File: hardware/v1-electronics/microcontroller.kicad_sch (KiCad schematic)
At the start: 8 parts, among them J1 USB_C_Receptacle_USB2.0_14P, U1 MDBT50Q-1MV2

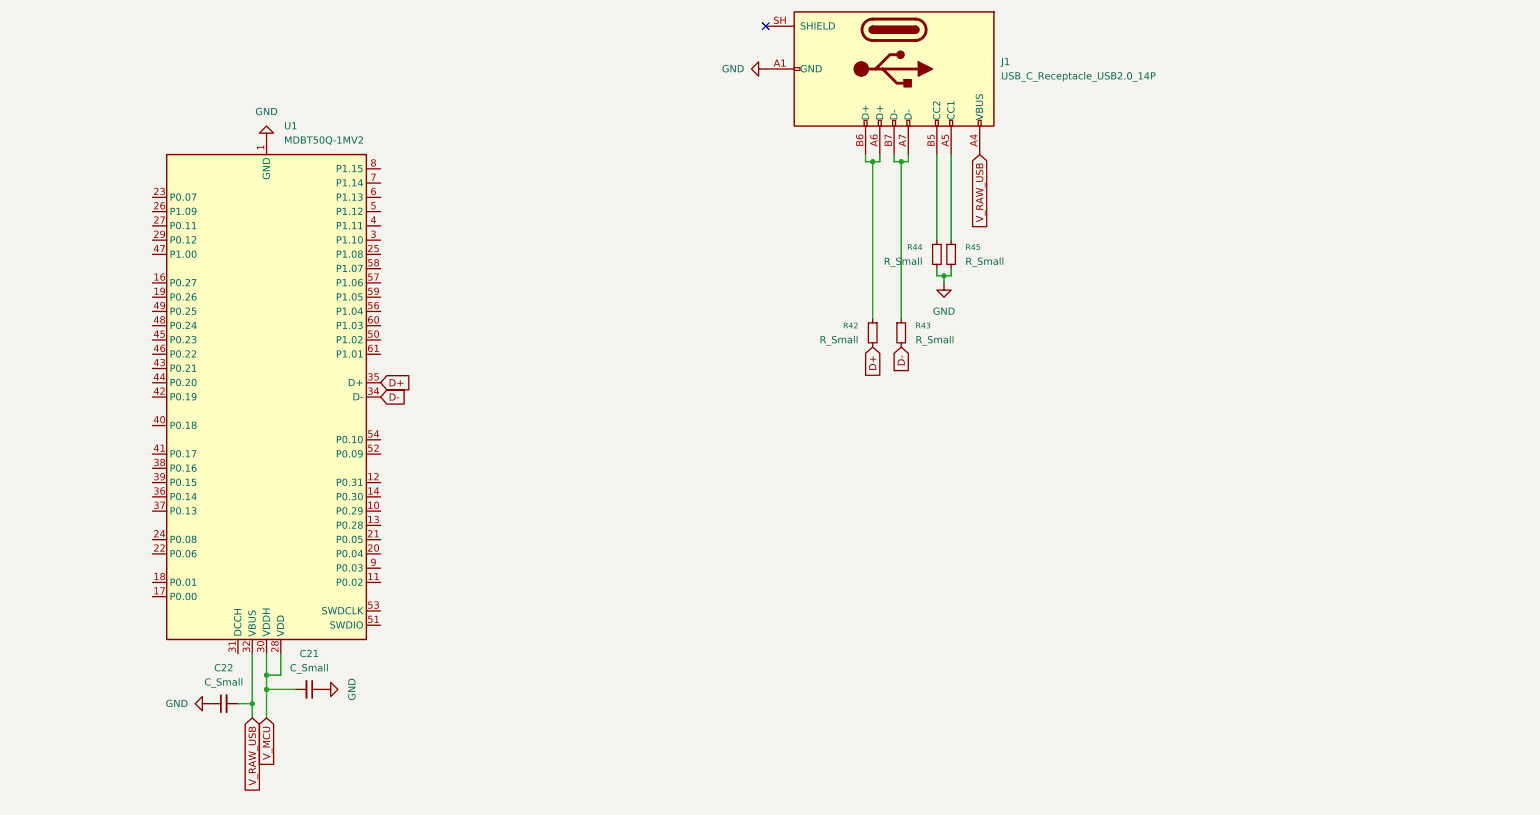
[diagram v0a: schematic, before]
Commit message: feat(v1 hardware): add simple power circuitry
I've added simple power circuitry. It does not do everything I want but
it's a start.
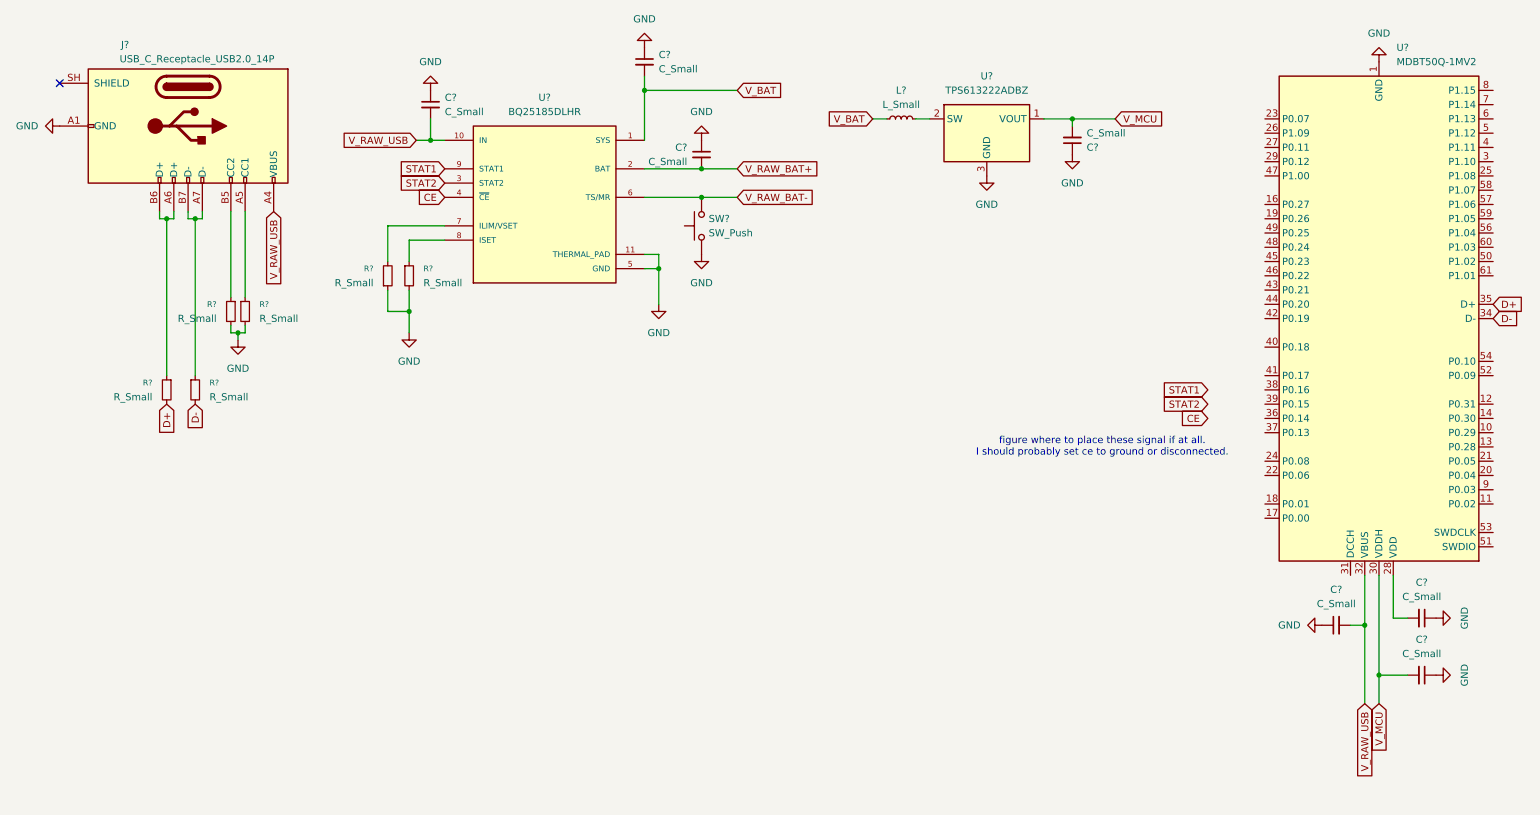
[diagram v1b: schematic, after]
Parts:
- added C? (x5): C_Small, symbol Device:C_Small
- added L?: L_Small, symbol Device:L_Small
- added R? (x2): R_Small, symbol Device:R_Small
- added SW?: SW_Push, symbol Switch:SW_Push
- added U?: TPS613222ADBZ, Package_TO_SOT_SMD:SOT-23, symbol Regulator_Switching:TPS613222ADBZ
- added U?: BQ25185DLHR, BQ25185DLHR:IC_BQ25185DLHR, symbol TI BQ25185DLHR:BQ25185DLHR
- renumbered C22 to C?, C21 to C?, J1 to J?, R42 to R?, R43 to R?, R44 to R?, R45 to R?, U1 to U?
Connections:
- net GND: now also C?.1, C?.1, C?.1, C?.1, C?.1, R?.1, R?.2, SW?.1, U?.11 (THERMAL_PAD), U?.3 (GND), U?.5 (GND)
- net V_MCU: now also C?.2, U?.1 (VOUT); no longer U?.28 (VDD)
- net V_RAW_USB: now also C?.2, U?.10 (IN)
- new net: R?.1, U?.8 (ISET)
- new net: R?.2, U?.7 (ILIM/VSET)
- new net: L?.2, U?.2 (SW)
- new net: C?.2, U?.28 (VDD)
- new net CE: U?.4 (~{CE})
- new net STAT1: U?.9 (STAT1)
- new net STAT2: U?.3 (STAT2)
- new net V_BAT: C?.2, L?.1, U?.1 (SYS)
- new net V_RAW_BAT+: C?.2, U?.2 (BAT)
- new net V_RAW_BAT-: SW?.2, U?.6 (TS/MR)
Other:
- note added: "figure where to place these signal if at all. I should probably set ce to ground or disconnected."
- moved on the sheet: C?, J?, R?, U?

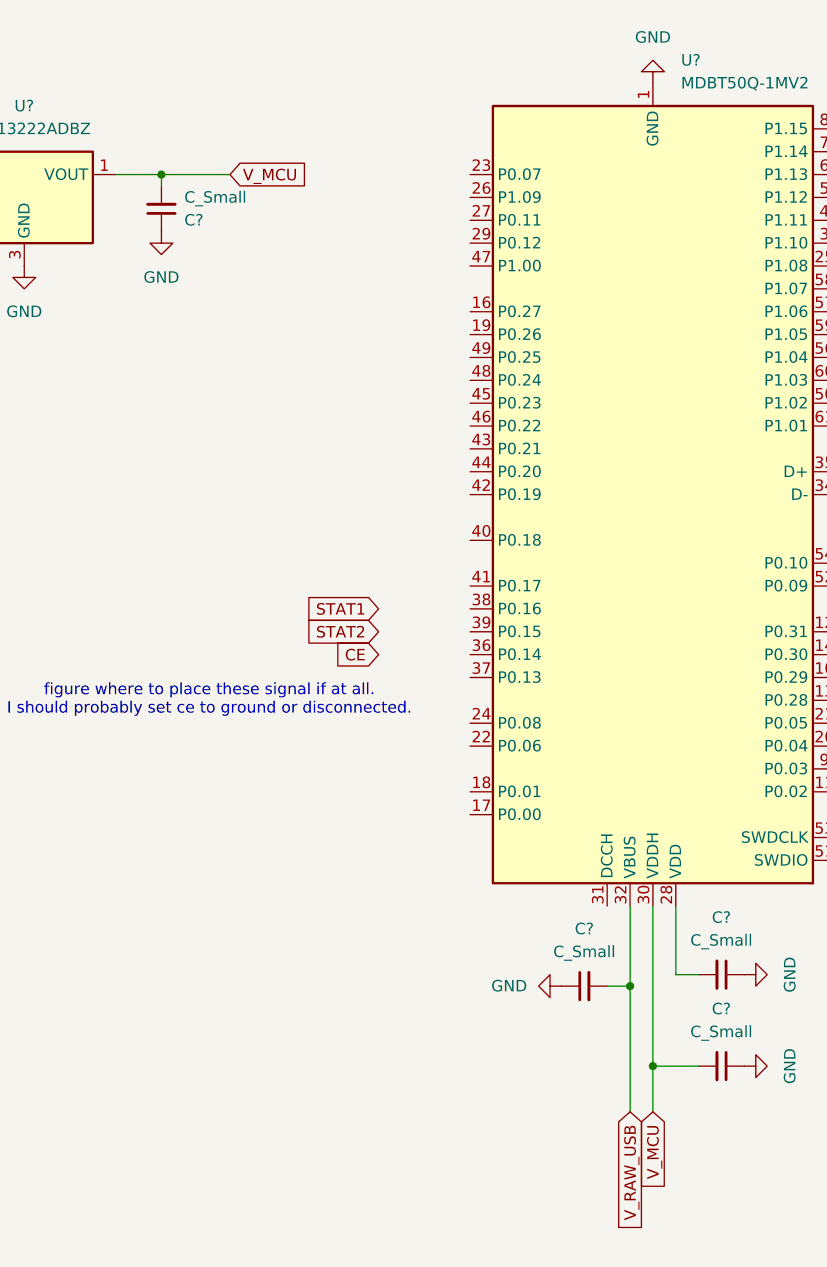
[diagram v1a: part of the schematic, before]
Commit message: feat(v1 hardware): LED Matrix
- added symbols and footprints for leds and their matrix ic.
- modified symbols for leds.
- started schematic for matrix ic and led matrix
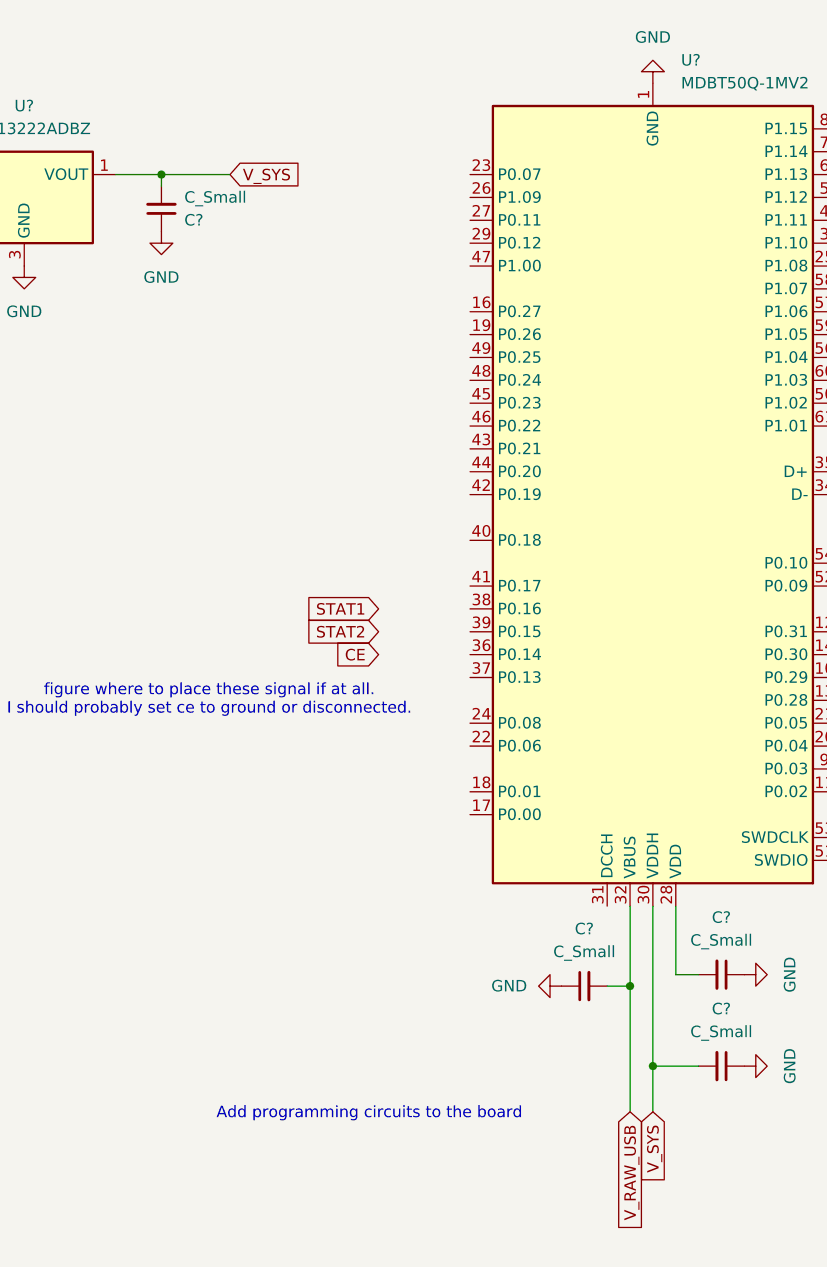
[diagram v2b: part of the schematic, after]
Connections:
- net V_MCU renamed V_SYS
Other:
- note added: "Add programming circuits to the board"
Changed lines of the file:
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@@
 	(generator_version "10.0")
 	(paper "A4")
+	(text "Add programming circuits to the board"
+		(exclude_from_sim no)
+		(at 225.044 141.224 0)
+		(effects
+			(font
+				(size 1.27 1.27)
+			)
+		)
+	)
 	(text "figure where to place these signal if at all.\nI should probably set ce to ground or disconnected."
 		(exclude_from_sim no)
@@
 		)
 	)
-	(global_label "V_MCU"
+	(global_label "V_SYS"
 		(shape input)
 		(at 209.55 36.83 0)
@@
 		)
 		(property "Intersheetrefs" "${INTERSHEET_REFS}"
-			(at 218.6433 36.83 0)
+			(at 218.099 36.83 0)
 			(hide yes)
 			(show_name no)
@@
 		)
 	)
-	(global_label "V_MCU"
+	(global_label "V_SYS"
 		(shape input)
 		(at 256.54 140.97 270)
@@
 		)
 		(property "Intersheetrefs" "${INTERSHEET_REFS}"
-			(at 256.54 150.0633 90)
-			(hide yes)
-			(show_name no)
+			(at 256.54 149.519 90)
+			(hide yes)
+			(show_name no)
